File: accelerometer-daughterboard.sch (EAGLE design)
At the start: 16 parts, among them Q2 BSS138, U1 LIS3DHTR

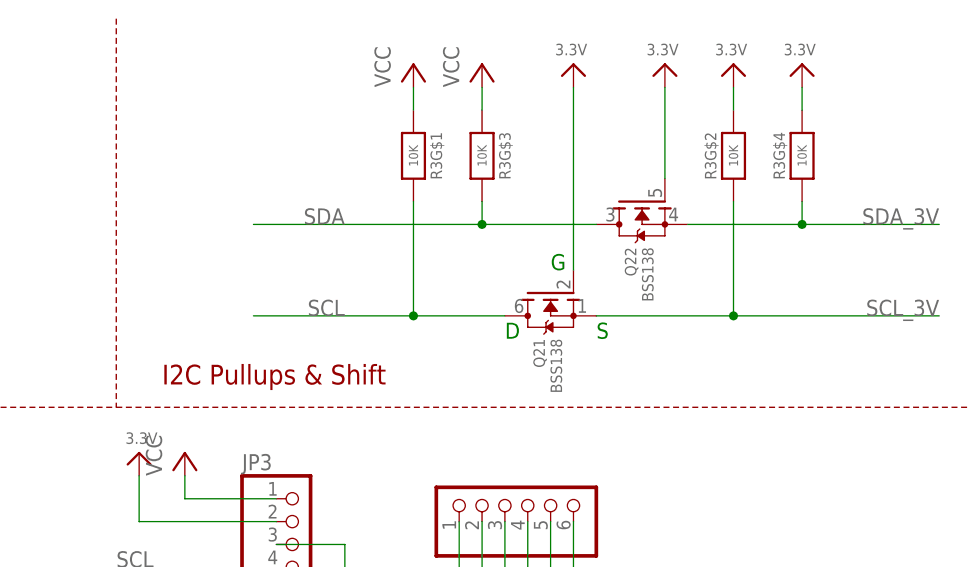
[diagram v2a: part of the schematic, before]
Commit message: Remove I2C level-shifting
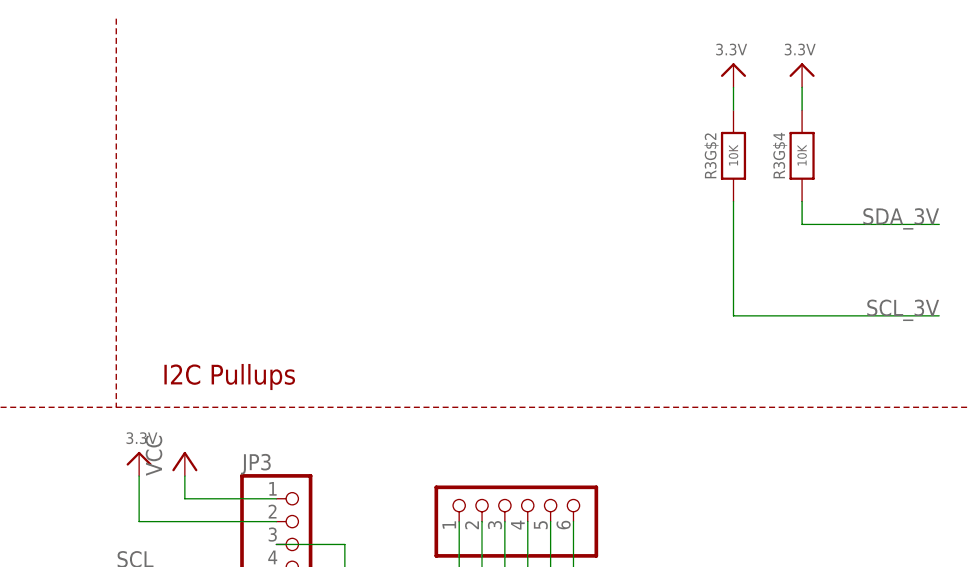
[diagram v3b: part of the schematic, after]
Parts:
- removed Q2: BSS138, microbuilder:MOSFET-N_DUAL
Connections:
- net 3.3V: no longer Q21.G, Q22.G
- net SCL: no longer Q21.D, R3G$1.2
- net SCL_3V: no longer Q21.S
- net SDA: no longer Q22.D, R3G$3.2
- net SDA_3V: no longer Q22.S
- net VCC: no longer R3G$1.1, R3G$3.1
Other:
- note added: "I2C Pullups"
- note removed: "D"
- note removed: "G"
- note removed: "I2C Pullups & Shift"
- note removed: "S"
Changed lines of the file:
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@@
 <part name="U$24" library="microbuilder" deviceset="3.3V" device=""/>
 <part name="R3" library="microbuilder" deviceset="RESISTOR_4PACK" device="" value="10K"/>
-<part name="Q2" library="microbuilder" deviceset="MOSFET-N_DUAL" device="" value="BSS138"/>
-<part name="U$26" library="microbuilder" deviceset="3.3V" device=""/>
-<part name="U$23" library="microbuilder" deviceset="3.3V" device=""/>
 <part name="U$1" library="microbuilder" deviceset="MOUNTINGHOLE" device="2.5"/>
 <part name="U$17" library="microbuilder" deviceset="MOUNTINGHOLE" device="2.5"/>
@@
 <part name="U$19" library="microbuilder" deviceset="MOUNTINGHOLE" device="2.5"/>
 <part name="U$21" library="microbuilder" deviceset="MOUNTINGHOLE" device="2.5"/>
-<part name="P+1" library="supply1" library_urn="urn:adsk.eagle:library:371" deviceset="VCC" device=""/>
-<part name="P+2" library="supply1" library_urn="urn:adsk.eagle:library:371" deviceset="VCC" device=""/>
 <part name="U1" library="microbuilder" deviceset="ACCEL_LIS3DHTR" device="" value="LIS3DHTR"/>
 <part name="U$2" library="microbuilder" deviceset="GND" device=""/>
@@
 <plain>
 <wire x1="2.54" y1="132.08" x2="68.58" y2="132.08" width="0.1524" layer="94" style="shortdash"/>
-<text x="93.98" y="134.62" size="2.1844" layer="94" ratio="7">I2C Pullups &amp; Shift</text>
+<text x="93.98" y="134.62" size="2.1844" layer="94" ratio="7">I2C Pullups</text>
 <text x="193.04" y="134.62" size="2.1844" layer="94" ratio="7">STEMMA/I2C Headers</text>
 <wire x1="68.58" y1="132.08" x2="88.9" y2="132.08" width="0.1524" layer="94" style="shortdash"/>
@@
 <wire x1="88.9" y1="175.26" x2="88.9" y2="132.08" width="0.1524" layer="94" style="shortdash"/>
 <wire x1="68.58" y1="175.26" x2="68.58" y2="132.08" width="0.1524" layer="94" style="shortdash"/>
-<text x="137.16" y="147.32" size="1.778" layer="91">G</text>
-<text x="142.24" y="139.7" size="1.778" layer="91">S</text>
-<text x="132.08" y="139.7" size="1.778" layer="91">D</text>
 <text x="177.8" y="76.2" size="1.778" layer="97">I2C</text>
 <text x="162.56" y="71.12" size="1.778" layer="97">SCL (Pin 4) = Serial Clock</text>
@@
 <attribute name="VALUE" x="157.48" y="160.02" size="1.016" layer="96" font="vector" ratio="15" rot="MR270" align="center"/>
 </instance>
-<instance part="Q2" gate="1" x="137.16" y="144.78" smashed="yes" rot="MR270">
-<attribute name="NAME" x="136.525" y="139.7" size="1.27" layer="95" rot="MR270"/>
-<attribute name="VALUE" x="138.43" y="139.7" size="1.27" layer="96" rot="MR270"/>
-</instance>
-<instance part="Q2" gate="2" x="147.32" y="154.94" smashed="yes" rot="MR270">
-<attribute name="NAME" x="146.685" y="149.86" size="1.27" layer="95" rot="MR270"/>
-<attribute name="VALUE" x="148.59" y="149.86" size="1.27" layer="96" rot="MR270"/>
-</instance>
-<instance part="U$26" gate="G$1" x="139.7" y="170.18" smashed="yes" rot="MR0">
-<attribute name="VALUE" x="141.224" y="171.196" size="1.27" layer="96" rot="MR0"/>
-</instance>
-<instance part="U$23" gate="G$1" x="149.86" y="170.18" smashed="yes" rot="MR0">
-<attribute name="VALUE" x="151.384" y="171.196" size="1.27" layer="96" rot="MR0"/>
-</instance>
-<instance part="R3" gate="G$3" x="129.54" y="160.02" smashed="yes" rot="R270">
-<attribute name="NAME" x="132.08" y="160.02" size="1.27" layer="95" font="vector" rot="R270" align="center"/>
-<attribute name="VALUE" x="129.54" y="160.02" size="1.016" layer="96" font="vector" ratio="15" rot="R270" align="center"/>
-</instance>
-<instance part="R3" gate="G$1" x="121.92" y="160.02" smashed="yes" rot="R270">
-<attribute name="NAME" x="124.46" y="160.02" size="1.27" layer="95" font="vector" rot="R270" align="center"/>
-<attribute name="VALUE" x="121.92" y="160.02" size="1.016" layer="96" font="vector" ratio="15" rot="R270" align="center"/>
-</instance>
-<instance part="P+1" gate="VCC" x="121.92" y="170.18" smashed="yes">
-<attribute name="VALUE" x="119.38" y="167.64" size="1.778" layer="96" rot="R90"/>
-</instance>
-<instance part="P+2" gate="VCC" x="129.54" y="170.18" smashed="yes">
-<attribute name="VALUE" x="127" y="167.64" size="1.778" layer="96" rot="R90"/>
-</instance>
 <instance part="U1" gate="G$1" x="104.14" y="63.5" smashed="yes">
 <attribute name="NAME" x="91.44" y="78.74" size="1.27" layer="95"/>
@@
 </segment>
 <segment>
-<wire x1="132.08" y1="142.24" x2="121.92" y2="142.24" width="0.1524" layer="91"/>
-<label x="114.3" y="142.24" size="1.778" layer="95" rot="MR0"/>
-<pinref part="Q2" gate="1" pin="D"/>
-<pinref part="R3" gate="G$1" pin="2"/>
-<wire x1="121.92" y1="142.24" x2="104.14" y2="142.24" width="0.1524" layer="91"/>
-<wire x1="121.92" y1="154.94" x2="121.92" y2="142.24" width="0.1524" layer="91"/>
-<junction x="121.92" y="142.24"/>
-</segment>
-<segment>
 <wire x1="106.68" y1="114.3" x2="88.9" y2="114.3" width="0.1524" layer="91"/>
 <label x="88.9" y="114.3" size="1.778" layer="95"/>
@@
 </segment>
 <segment>
-<wire x1="142.24" y1="152.4" x2="129.54" y2="152.4" width="0.1524" layer="91"/>
-<label x="114.3" y="152.4" size="1.778" layer="95" rot="MR0"/>
-<pinref part="Q2" gate="2" pin="D"/>
-<pinref part="R3" gate="G$3" pin="2"/>
-<wire x1="129.54" y1="152.4" x2="104.14" y2="152.4" width="0.1524" layer="91"/>
-<wire x1="129.54" y1="154.94" x2="129.54" y2="152.4" width="0.1524" layer="91"/>
-<junction x="129.54" y="152.4"/>
-</segment>
-<segment>
 <wire x1="106.68" y1="111.76" x2="88.9" y2="111.76" width="0.1524" layer="91"/>
 <label x="88.9" y="111.76" size="1.778" layer="95"/>
@@
 </segment>
 <segment>
-<pinref part="R3" gate="G$1" pin="1"/>
-<wire x1="121.92" y1="167.64" x2="121.92" y2="165.1" width="0.1524" layer="91"/>
-<pinref part="P+1" gate="VCC" pin="VCC"/>
-</segment>
-<segment>
-<pinref part="R3" gate="G$3" pin="1"/>
-<wire x1="129.54" y1="165.1" x2="129.54" y2="167.64" width="0.1524" layer="91"/>
-<pinref part="P+2" gate="VCC" pin="VCC"/>
-</segment>
-<segment>
 <wire x1="106.68" y1="121.92" x2="96.52" y2="121.92" width="0.1524" layer="91"/>
 <wire x1="96.52" y1="121.92" x2="96.52" y2="124.46" width="0.1524" layer="91"/>
@@
 <net name="SCL_3V" class="0">
 <segment>
-<wire x1="142.24" y1="142.24" x2="157.48" y2="142.24" width="0.1524" layer="91"/>
 <label x="180.34" y="142.24" size="1.778" layer="95" rot="MR0"/>
 <wire x1="157.48" y1="142.24" x2="180.34" y2="142.24" width="0.1524" layer="91"/>
 <wire x1="157.48" y1="154.94" x2="157.48" y2="142.24" width="0.1524" layer="91"/>
-<junction x="157.48" y="142.24"/>
 <pinref part="R3" gate="G$2" pin="2"/>
-<pinref part="Q2" gate="1" pin="S"/>
 </segment>
 <segment>
@@
 <net name="SDA_3V" class="0">
 <segment>
-<wire x1="152.4" y1="152.4" x2="165.1" y2="152.4" width="0.1524" layer="91"/>
 <label x="180.34" y="152.4" size="1.778" layer="95" rot="MR0"/>
 <wire x1="165.1" y1="152.4" x2="180.34" y2="152.4" width="0.1524" layer="91"/>
 <wire x1="165.1" y1="154.94" x2="165.1" y2="152.4" width="0.1524" layer="91"/>
-<junction x="165.1" y="152.4"/>
 <pinref part="R3" gate="G$4" pin="2"/>
-<pinref part="Q2" gate="2" pin="S"/>
 </segment>
 <segment>
@@
 </segment>
 <segment>
-<pinref part="U$26" gate="G$1" pin="3.3V"/>
-<wire x1="139.7" y1="147.32" x2="139.7" y2="167.64" width="0.1524" layer="91"/>
-<pinref part="Q2" gate="1" pin="G"/>
-</segment>
-<segment>
 <pinref part="U$24" gate="G$1" pin="3.3V"/>
 <wire x1="157.48" y1="165.1" x2="157.48" y2="167.64" width="0.1524" layer="91"/>
@@
 </segment>
 <segment>
-<wire x1="149.86" y1="157.48" x2="149.86" y2="167.64" width="0.1524" layer="91"/>
-<pinref part="Q2" gate="2" pin="G"/>
-<pinref part="U$23" gate="G$1" pin="3.3V"/>
-</segment>
-<segment>

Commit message: Remove connector headers
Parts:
- removed CONN3, CONN4: STEMMA_I2C_QT, microbuilder:STEMMA_I2C_QT
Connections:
- net GND: no longer CONN3G$1.GND, CONN4G$1.GND
- net SCL: no longer CONN3G$1.SCL, CONN4G$1.SCL
- net SDA: no longer CONN3G$1.SDA, CONN4G$1.SDA
- net VCC: no longer CONN3G$1.V+, CONN4G$1.V+
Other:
- note removed: "STEMMA/I2C Headers"
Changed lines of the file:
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@@
 <part name="U$1" library="microbuilder" deviceset="MOUNTINGHOLE" device="2.5"/>
 <part name="U$17" library="microbuilder" deviceset="MOUNTINGHOLE" device="2.5"/>
-<part name="CONN3" library="microbuilder" deviceset="STEMMA_I2C" device="_QT"/>
-<part name="CONN4" library="microbuilder" deviceset="STEMMA_I2C" device="_QT"/>
 <part name="U$18" library="microbuilder" deviceset="FRAME_A4_ADAFRUIT" device=""/>
 <part name="FID3" library="microbuilder" deviceset="FIDUCIAL" device="_1MM"/>
@@
 <wire x1="2.54" y1="132.08" x2="68.58" y2="132.08" width="0.1524" layer="94" style="shortdash"/>
 <text x="93.98" y="134.62" size="2.1844" layer="94" ratio="7">I2C Pullups</text>
-<text x="193.04" y="134.62" size="2.1844" layer="94" ratio="7">STEMMA/I2C Headers</text>
 <wire x1="68.58" y1="132.08" x2="88.9" y2="132.08" width="0.1524" layer="94" style="shortdash"/>
 <wire x1="88.9" y1="132.08" x2="190.5" y2="132.08" width="0.1524" layer="94" style="shortdash"/>
@@
 <instance part="U$1" gate="G$1" x="243.84" y="22.86" smashed="yes"/>
 <instance part="U$17" gate="G$1" x="243.84" y="30.48" smashed="yes"/>
-<instance part="CONN3" gate="G$1" x="205.74" y="152.4" smashed="yes">
-<attribute name="NAME" x="201.93" y="160.655" size="1.778" layer="95"/>
-<attribute name="VALUE" x="201.93" y="144.78" size="1.778" layer="96"/>
-</instance>
-<instance part="CONN4" gate="G$1" x="238.76" y="152.4" smashed="yes">
-<attribute name="NAME" x="234.95" y="160.655" size="1.778" layer="95"/>
-<attribute name="VALUE" x="234.95" y="144.78" size="1.778" layer="96"/>
-</instance>
 <instance part="U$18" gate="G$1" x="0" y="0" smashed="yes">
 <attribute name="DRAWING_NAME" x="171.45" y="15.24" size="2.54" layer="94" font="vector"/>
@@
 <net name="GND" class="1">
 <segment>
-<pinref part="CONN4" gate="G$1" pin="GND"/>
-<pinref part="CONN3" gate="G$1" pin="GND"/>
-<wire x1="238.76" y1="157.48" x2="205.74" y2="157.48" width="0.1524" layer="91"/>
-<label x="220.98" y="157.48" size="1.778" layer="95"/>
-</segment>
-<segment>
 <pinref part="U1" gate="G$1" pin="GND@1"/>
 <pinref part="U$2" gate="G$1" pin="GND"/>
@@
 <net name="SCL" class="0">
 <segment>
-<pinref part="CONN4" gate="G$1" pin="SCL"/>
-<pinref part="CONN3" gate="G$1" pin="SCL"/>
-<wire x1="205.74" y1="149.86" x2="238.76" y2="149.86" width="0.1524" layer="91"/>
-<label x="220.98" y="149.86" size="1.778" layer="95"/>
-</segment>
-<segment>
 <wire x1="106.68" y1="114.3" x2="88.9" y2="114.3" width="0.1524" layer="91"/>
 <label x="88.9" y="114.3" size="1.778" layer="95"/>
@@
 </net>
 <net name="SDA" class="0">
-<segment>
-<pinref part="CONN4" gate="G$1" pin="SDA"/>
-<pinref part="CONN3" gate="G$1" pin="SDA"/>
-<wire x1="238.76" y1="152.4" x2="205.74" y2="152.4" width="0.1524" layer="91"/>
-<label x="220.98" y="152.4" size="1.778" layer="95"/>
-</segment>
 <segment>
 <wire x1="106.68" y1="111.76" x2="88.9" y2="111.76" width="0.1524" layer="91"/>
@@
 <net name="VCC" class="1">
 <segment>
-<pinref part="CONN3" gate="G$1" pin="V+"/>
-<pinref part="CONN4" gate="G$1" pin="V+"/>
-<wire x1="205.74" y1="154.94" x2="238.76" y2="154.94" width="0.1524" layer="91"/>
-<label x="220.98" y="154.94" size="1.778" layer="95"/>
-</segment>
-<segment>
 <wire x1="106.68" y1="121.92" x2="96.52" y2="121.92" width="0.1524" layer="91"/>

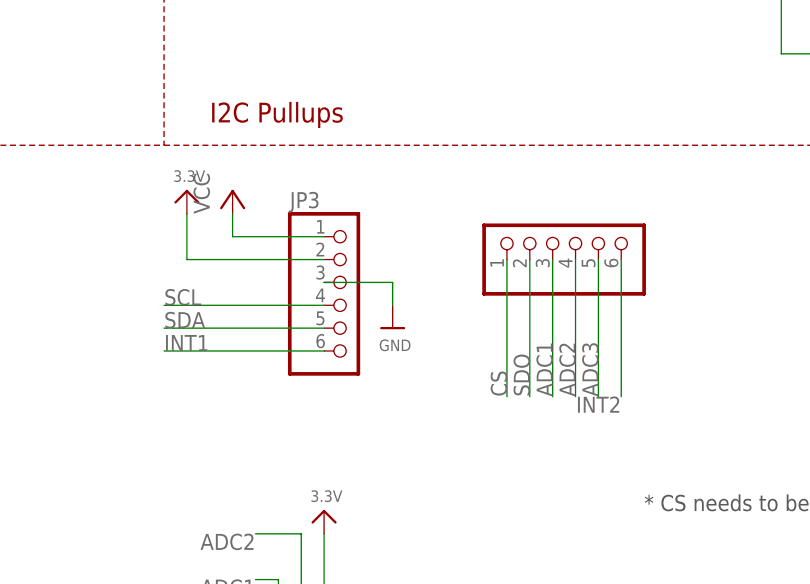
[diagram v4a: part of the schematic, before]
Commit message: Remove through-holes
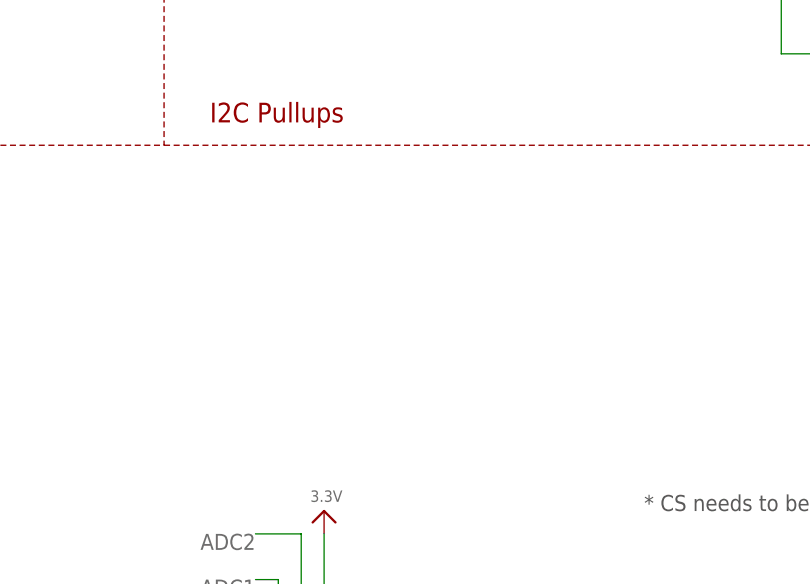
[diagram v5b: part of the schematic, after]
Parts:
- removed JP2, JP3: (no value), microbuilder:HEADER-1X670MIL
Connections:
- removed net SCL: JP3.4
- removed net SDA: JP3.5
- removed net VCC: JP3.1
- net 3.3V: no longer JP3.2
- net ADC1: no longer JP2.3
- net ADC2: no longer JP2.4
- net ADC3: no longer JP2.5
- net CS: no longer JP2.1
- net GND: no longer JP3.3
- net INT1: no longer JP3.6
- net INT2: no longer JP2.6
- net SDO: no longer JP2.2
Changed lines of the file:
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@@
 <part name="U$20" library="microbuilder" deviceset="3.3V" device=""/>
 <part name="U$27" library="microbuilder" deviceset="GND" device=""/>
-<part name="U$28" library="microbuilder" deviceset="3.3V" device=""/>
-<part name="U$29" library="microbuilder" deviceset="GND" device=""/>
-<part name="JP3" library="microbuilder" deviceset="HEADER-1X6" device="70MIL"/>
-<part name="P+4" library="supply1" library_urn="urn:adsk.eagle:library:371" deviceset="VCC" device=""/>
 <part name="R1" library="microbuilder" deviceset="RESISTOR_4PACK" device="" value="10K"/>
-<part name="JP2" library="microbuilder" deviceset="HEADER-1X6" device="70MIL"/>
 <part name="U$9" library="microbuilder" deviceset="3.3V" device=""/>
 <part name="U$10" library="microbuilder" deviceset="3.3V" device=""/>
@@
 <attribute name="VALUE" x="133.096" y="22.86" size="1.27" layer="96"/>
 </instance>
-<instance part="U$28" gate="G$1" x="91.44" y="127" smashed="yes">
-<attribute name="VALUE" x="89.916" y="128.016" size="1.27" layer="96"/>
-</instance>
-<instance part="U$29" gate="G$1" x="114.3" y="111.76" smashed="yes">
-<attribute name="VALUE" x="112.776" y="109.22" size="1.27" layer="96"/>
-</instance>
-<instance part="JP3" gate="A" x="109.22" y="114.3" smashed="yes">
-<attribute name="NAME" x="102.87" y="125.095" size="1.778" layer="95"/>
-<attribute name="VALUE" x="102.87" y="104.14" size="1.778" layer="96"/>
-</instance>
-<instance part="P+4" gate="VCC" x="96.52" y="127" smashed="yes">
-<attribute name="VALUE" x="93.98" y="124.46" size="1.778" layer="96" rot="R90"/>
-</instance>
 <instance part="R1" gate="G$1" x="45.72" y="101.6" smashed="yes" rot="R90">
 <attribute name="NAME" x="43.18" y="101.6" size="1.27" layer="95" font="vector" rot="R90" align="center"/>
@@
 <attribute name="NAME" x="132.08" y="43.18" size="1.27" layer="95" font="vector" rot="R90" align="center"/>
 <attribute name="VALUE" x="134.62" y="43.18" size="1.016" layer="96" font="vector" ratio="15" rot="R90" align="center"/>
-</instance>
-<instance part="JP2" gate="A" x="134.62" y="121.92" smashed="yes" rot="R90">
-<attribute name="VALUE" x="144.78" y="115.57" size="1.778" layer="96" rot="R90"/>
 </instance>
 <instance part="U$9" gate="G$1" x="45.72" y="109.22" smashed="yes">
@@
 <pinref part="R1" gate="G$3" pin="2"/>
 </segment>
-<segment>
-<pinref part="U$29" gate="G$1" pin="GND"/>
-<wire x1="106.68" y1="116.84" x2="114.3" y2="116.84" width="0.1524" layer="91"/>
-<wire x1="114.3" y1="116.84" x2="114.3" y2="114.3" width="0.1524" layer="91"/>
-<pinref part="JP3" gate="A" pin="3"/>
-</segment>
-</net>
-<net name="SCL" class="0">
-<segment>
-<wire x1="106.68" y1="114.3" x2="88.9" y2="114.3" width="0.1524" layer="91"/>
-<label x="88.9" y="114.3" size="1.778" layer="95"/>
-<pinref part="JP3" gate="A" pin="4"/>
-</segment>
-</net>
-<net name="SDA" class="0">
-<segment>
-<wire x1="106.68" y1="111.76" x2="88.9" y2="111.76" width="0.1524" layer="91"/>
-<label x="88.9" y="111.76" size="1.778" layer="95"/>
-<pinref part="JP3" gate="A" pin="5"/>
-</segment>
-</net>
-<net name="VCC" class="1">
-<segment>
-<wire x1="106.68" y1="121.92" x2="96.52" y2="121.92" width="0.1524" layer="91"/>
-<wire x1="96.52" y1="121.92" x2="96.52" y2="124.46" width="0.1524" layer="91"/>
-<pinref part="JP3" gate="A" pin="1"/>
-<pinref part="P+4" gate="VCC" pin="VCC"/>
-</segment>
 </net>
 <net name="SCL_3V" class="0">
@@
 </segment>
 <segment>
-<pinref part="U$28" gate="G$1" pin="3.3V"/>
-<wire x1="106.68" y1="119.38" x2="91.44" y2="119.38" width="0.1524" layer="91"/>
-<wire x1="91.44" y1="119.38" x2="91.44" y2="124.46" width="0.1524" layer="91"/>
-<pinref part="JP3" gate="A" pin="2"/>
-</segment>
-<segment>
 <pinref part="R1" gate="G$1" pin="2"/>
 <pinref part="U$9" gate="G$1" pin="3.3V"/>
@@
 <wire x1="86.36" y1="27.94" x2="71.12" y2="27.94" width="0.1524" layer="91"/>
 <label x="71.12" y="27.94" size="1.778" layer="95"/>
-</segment>
-<segment>
-<wire x1="127" y1="104.14" x2="127" y2="119.38" width="0.1524" layer="91"/>
-<label x="127" y="104.14" size="1.778" layer="95" rot="R90"/>
-<pinref part="JP2" gate="A" pin="1"/>
 </segment>
 </net>
@@
 <label x="121.92" y="63.5" size="1.778" layer="95"/>
 </segment>
-<segment>
-<wire x1="106.68" y1="109.22" x2="88.9" y2="109.22" width="0.1524" layer="91"/>
-<label x="88.9" y="109.22" size="1.778" layer="95"/>
-<pinref part="JP3" gate="A" pin="6"/>
-</segment>
 </net>
 <net name="SDO" class="0">
@@
 <junction x="116.84" y="33.02"/>
 </segment>
-<segment>
-<wire x1="129.54" y1="119.38" x2="129.54" y2="104.14" width="0.1524" layer="91"/>
-<label x="129.54" y="104.14" size="1.778" layer="95" rot="R90"/>
-<pinref part="JP2" gate="A" pin="2"/>
-</segment>
 </net>
 <net name="ADC1" class="0">
@@
 <label x="99.06" y="83.82" size="1.778" layer="95" rot="R180"/>
 </segment>
-<segment>
-<wire x1="132.08" y1="119.38" x2="132.08" y2="104.14" width="0.1524" layer="91"/>
-<label x="132.08" y="104.14" size="1.778" layer="95" rot="R90"/>
-<pinref part="JP2" gate="A" pin="3"/>
-</segment>
 </net>
 <net name="ADC2" class="0">
@@
 <label x="99.06" y="88.9" size="1.778" layer="95" rot="R180"/>
 </segment>
-<segment>
-<wire x1="134.62" y1="104.14" x2="134.62" y2="119.38" width="0.1524" layer="91"/>
-<label x="134.62" y="104.14" size="1.778" layer="95" rot="R90"/>
-<pinref part="JP2" gate="A" pin="4"/>
-</segment>
 </net>
 <net name="ADC3" class="0">
@@
 <label x="121.92" y="68.58" size="1.778" layer="95"/>
 </segment>
-<segment>
-<wire x1="137.16" y1="119.38" x2="137.16" y2="104.14" width="0.1524" layer="91"/>
-<label x="137.16" y="104.14" size="1.778" layer="95" rot="R90"/>
-<pinref part="JP2" gate="A" pin="5"/>
-</segment>
 </net>
 <net name="INT2" class="0">
@@
 <wire x1="119.38" y1="58.42" x2="127" y2="58.42" width="0.1524" layer="91"/>
 <label x="121.92" y="58.42" size="1.778" layer="95"/>
-</segment>
-<segment>
-<pinref part="JP2" gate="A" pin="6"/>
-<wire x1="139.7" y1="119.38" x2="139.7" y2="104.14" width="0.1524" layer="91"/>
-<label x="139.7" y="104.14" size="1.778" layer="95" rot="R180"/>
 </segment>
 </net>
@@
 </schematic>
 </drawing>
-<compatibility>
-<note version="8.2" severity="warning">
-Since Version 8.2, EAGLE supports online libraries. The ids
-of those online libraries will not be understood (or retained)
-with this version.
-</note>
-<note version="8.3" severity="warning">
-Since Version 8.3, EAGLE supports URNs for individual library
-assets (packages, symbols, and devices). The URNs of those assets
-will not be understood (or retained) with this version.
-</note>
-</compatibility>
 </eagle>
